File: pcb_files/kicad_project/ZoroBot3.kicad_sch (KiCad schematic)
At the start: 107 parts, among them SW1 SW_Push, SW2 SW_Push, SW3 SW_Push, SW4 SW_DIP_x02, SW5 SW_Reset, U1 TB6612FNG, U3 MP2307, Y1 Crystal

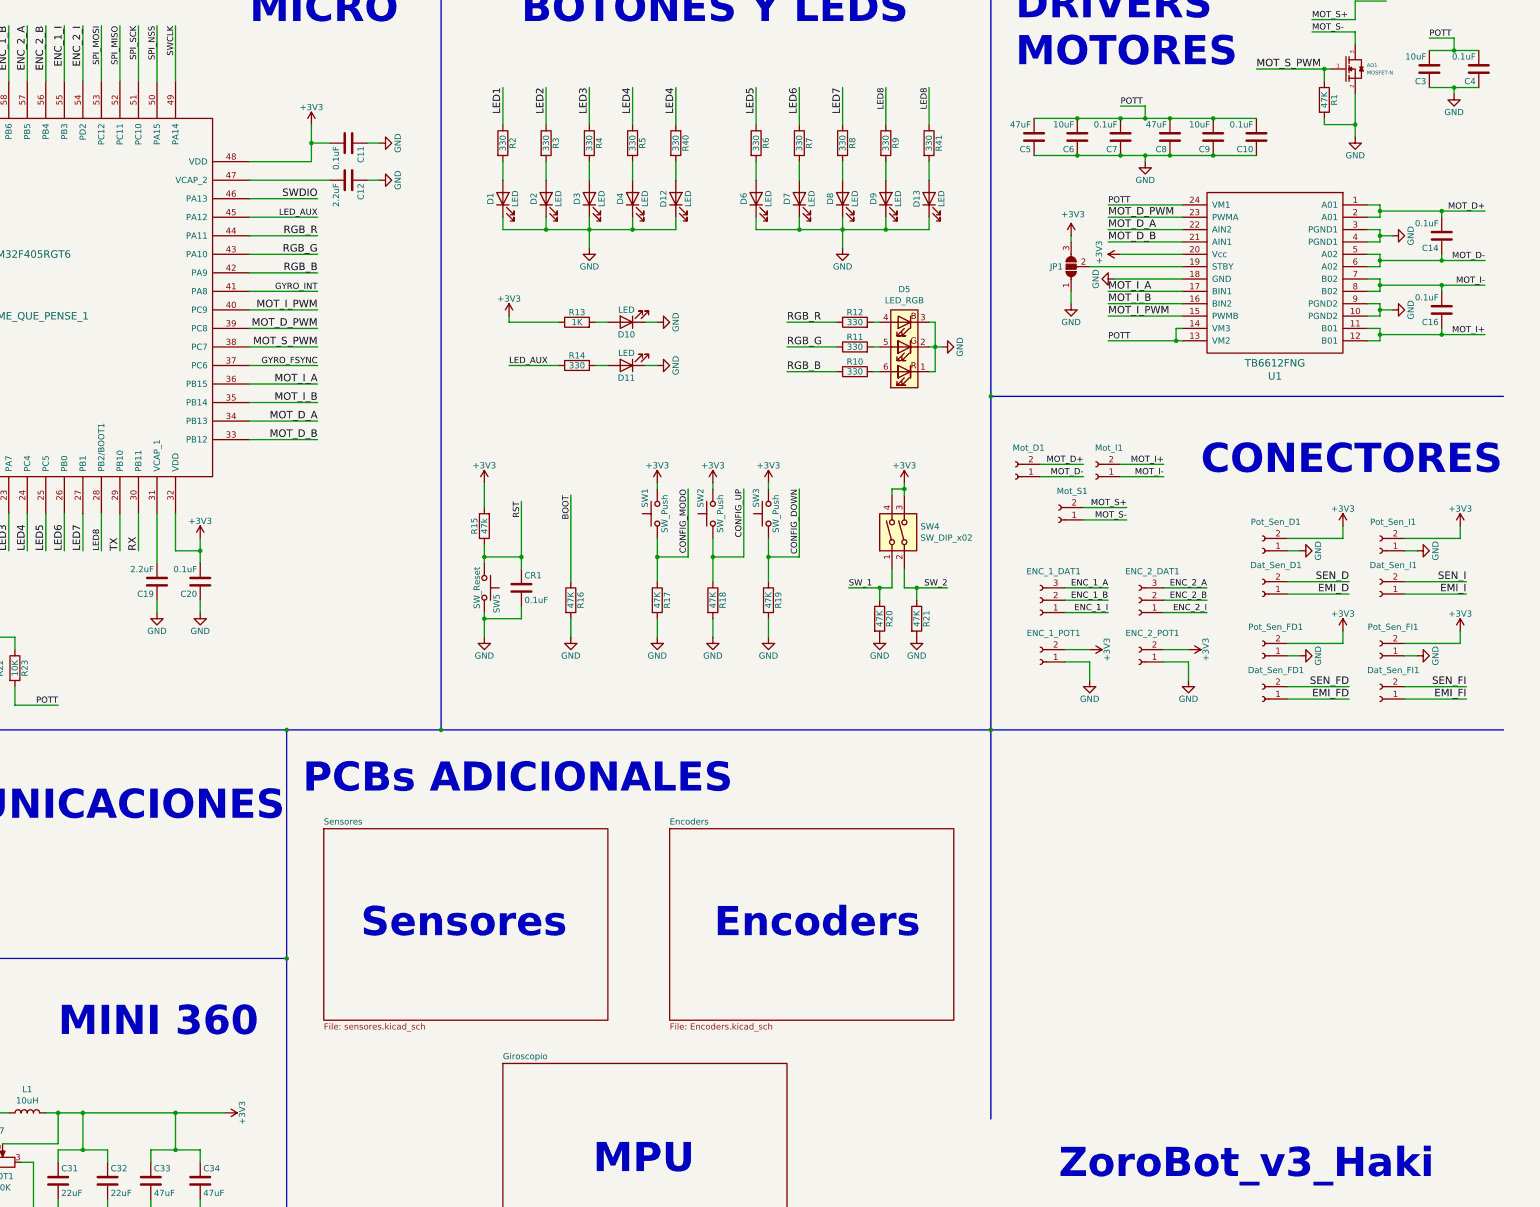
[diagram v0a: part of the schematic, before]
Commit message: Añade nuevo MPU LSM6DSR
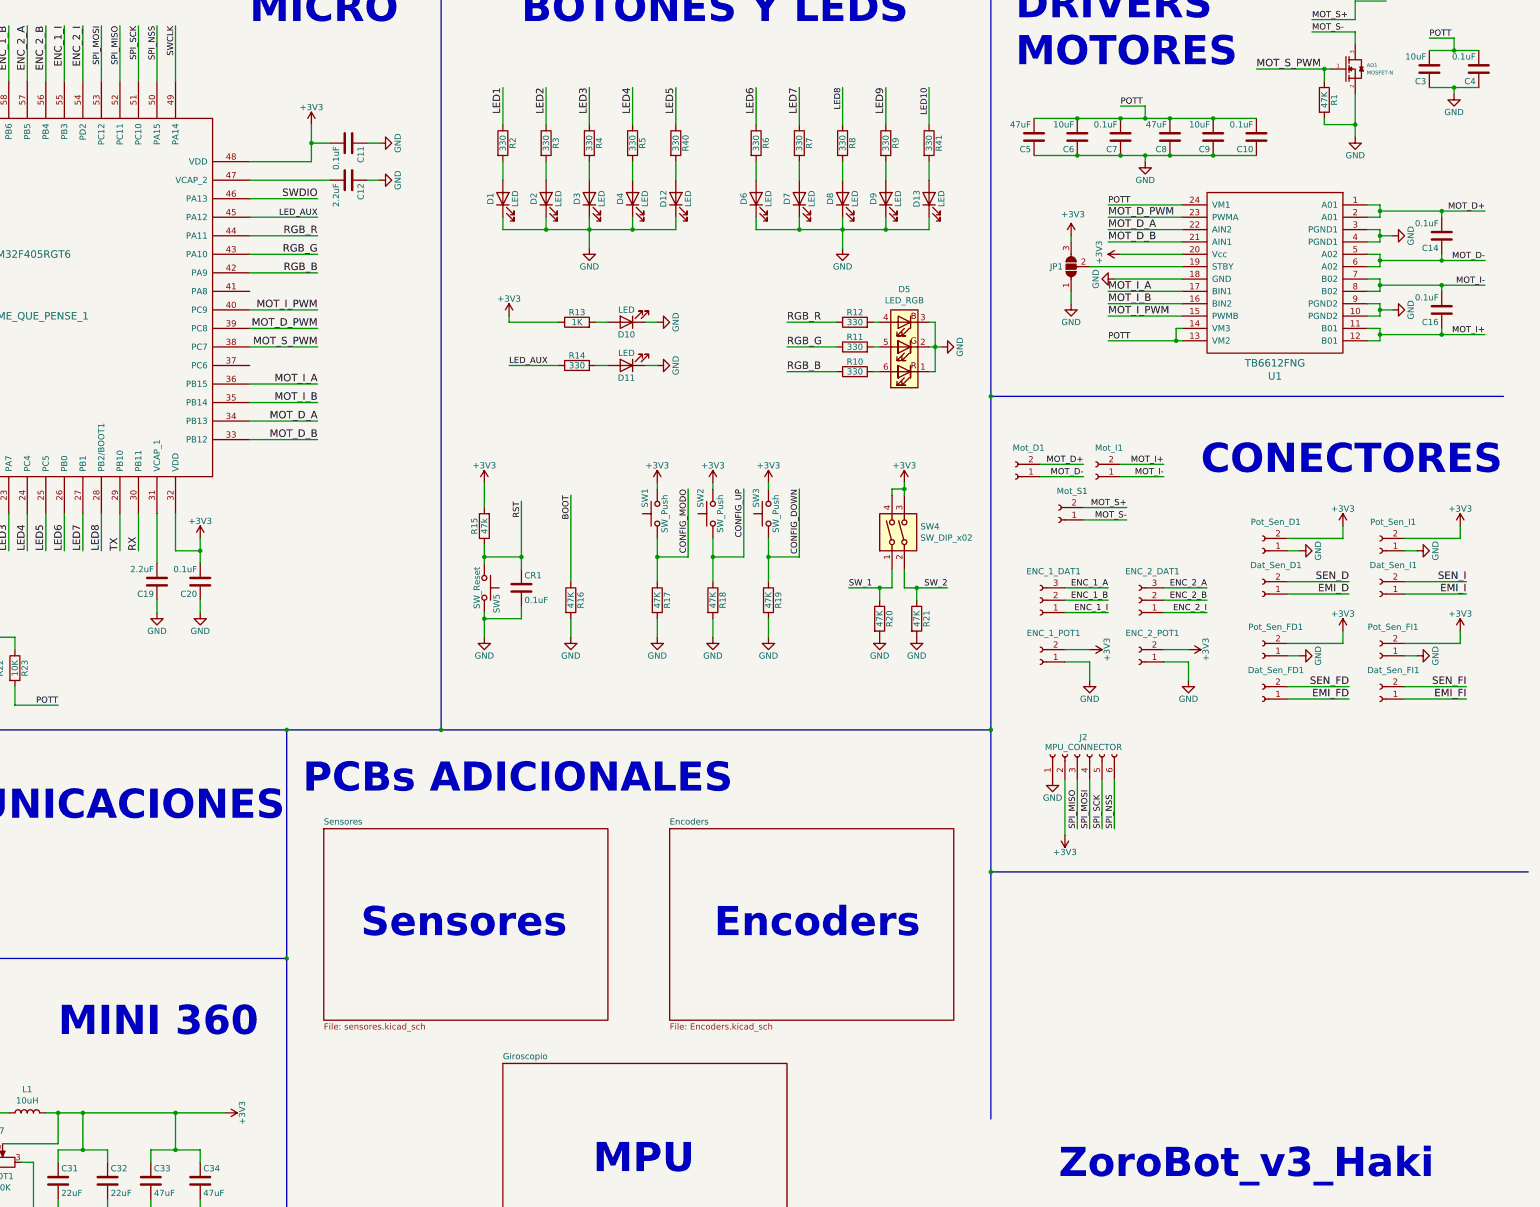
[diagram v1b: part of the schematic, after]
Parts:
- added J2: MPU_CONNECTOR, symbol Connector:Conn_01x06_Socket
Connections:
- net +3V3: now also J2.2 (Pin_2)
- net GND: now also J2.1 (Pin_1)
- net LED4: no longer R40.1
- net LED5: now also R40.1; no longer R6.1
- net LED6: now also R6.1; no longer R7.1
- net LED7: now also R7.1; no longer R8.1
- net LED8: now also R8.1; no longer R41.1, R9.1
- net SPI_MISO: now also J2.3 (Pin_3)
- net SPI_MOSI: now also J2.4 (Pin_4)
- net SPI_NSS: now also J2.6 (Pin_6)
- net SPI_SCK: now also J2.5 (Pin_5)
- net GYRO_FSYNC: no longer names the net of DEIXAME_QUE_PENSE_1.37 (PC6)
- net GYRO_INT: no longer names the net of DEIXAME_QUE_PENSE_1.41 (PA8)
- new net LED10: R41.1
- new net LED9: R9.1

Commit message: Añade receptor IR SMD TSSP77038TR
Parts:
- removed SW1, SW2, SW3: SW_Push, Button_Switch_SMD:SW_SPST_EVQPE1, symbol PCB_ZoroBot_v3-rescue:SW_Push-multiPCB-rescue-multiPCB-rescue-PCB_Fujitora-resc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
- removed SW4: SW_DIP_x02, Button_Switch_SMD:SW_DIP_SPSTx02_Slide_6.7x6.64mm_W8.61mm_P2.54mm_LowProfile, symbol Switch:SW_DIP_x02
- added AO4, AO5: MOSFET-N, Package_TO_SOT_SMD:SOT-23, symbol PCB_ZoroBot_v3-rescue:MOSFET-N-MOSFET-N
- added BATT_1: Conn_01x02_Female, custom_footprints:XT30 connector, symbol PCB_Fujitora-rescue:Conn_01x02_Female-Connector
- added BTN1, BTN2, BTN3: ~, Button_Switch_SMD:SW_Push_1P1T_NO_6x6mm_H9.5mm, symbol custom_symbols:Button
- added C49: 10uF, Capacitor_SMD:C_0805_2012Metric, symbol Device:C
- added C50, CR5, CR6: 0.1uF, Capacitor_SMD:C_0805_2012Metric, symbol Device:C
- added C51, C52, C53, CR2: 0.1uF, Capacitor_SMD:C_0805_2012Metric_Pad1.18x1.45mm_HandSolder, symbol Device:C
- added CR3, CR4: 0.1uF, Capacitor_SMD:C_0402_1005Metric_Pad0.74x0.62mm_HandSolder, symbol Device:C
- added D14: D, Diode_SMD:D_1206_3216Metric, symbol Device:D
- added DC-DC1: ~, custom_footprints:SOP8_with_gnd_pad, symbol custom_symbols:CN3903
- added IR_RECIVER1: ~, symbol custom_symbols:TSSP77038TR
- added L2: L, Inductor_SMD:L_Wuerth_HCM-7050, symbol Device:L
- added MIC5219: ~, Package_TO_SOT_SMD:SOT-23-5_HandSoldering, symbol custom_symbols:LDO_ME611C33
- added MSK12C2: SW_DPDT_x2, libs sueltas:MSK12C2, symbol Switch:SW_DPDT_x2
- added R29: 47K, Resistor_SMD:R_0805_2012Metric_Pad1.20x1.40mm_HandSolder, symbol Device:R
- added R30: 47K, Resistor_SMD:R_0805_2012Metric, symbol Device:R
- R16: value 47K -> 45K; footprint Resistor_SMD:R_0805_2012Metric -> Resistor_SMD:R_0402_1005Metric_Pad0.72x0.64mm_HandSolder
- R18: value 47K -> 100k; footprint Resistor_SMD:R_0805_2012Metric -> Resistor_SMD:R_0402_1005Metric_Pad0.72x0.64mm_HandSolder
- R19: value 47K -> 60k; footprint Resistor_SMD:R_0805_2012Metric -> Resistor_SMD:R_0402_1005Metric_Pad0.72x0.64mm_HandSolder
- R20: value 47K -> 100K; footprint Resistor_SMD:R_0805_2012Metric -> Resistor_SMD:R_0805_2012Metric_Pad1.20x1.40mm_HandSolder
- R21: footprint Resistor_SMD:R_0805_2012Metric -> Resistor_SMD:R_0805_2012Metric_Pad1.20x1.40mm_HandSolder
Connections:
- net SW_1 is gone; now on net CONFIG_MODO: R20.1
- net SW_2 is gone; now on net CONFIG_UP: R21.1
- net +3V3: now also C49.2, C50.2, IR_RECIVER1.2 (VCC)
- net BOOT: now also R17.1; no longer R16.1
- net CONFIG_DOWN: now also BTN3.1, C53.1, R29.1; no longer R19.1
- net CONFIG_MODO: now also BTN1.1, C51.1; no longer R17.1
- net CONFIG_UP: now also BTN2.1, C52.1; no longer R18.1
- net GND: now also R16.1, AO5.2, BATT_1.1 (Pin_1), C49.1, C50.1, C51.2, C52.2, C53.2, CR2.1, CR5.1, CR6.2, D14.2 (A), DC-DC1.4 (GND), DC-DC1.9 (EPAD), IR_RECIVER1.1 (GND), IR_RECIVER1.4 (GND), MIC5219.2 (VSS), R29.2, R30.2; no longer R16.2, R18.2, R19.2
- net LED10: now also DEIXAME_QUE_PENSE_1.61 (PB8)
- net LED9: now also DEIXAME_QUE_PENSE_1.62 (PB9)
- net LED_AUX: now also DEIXAME_QUE_PENSE_1.41 (PA8); no longer DEIXAME_QUE_PENSE_1.45 (PA12)
- net MOT_S-: now also AO5.3
- net MOT_S_PWM: now also AO5.1, R30.1
- net at MOSFET-P1.1, R25.2: no longer MSK12C1.3 (C)
- net AUX_PIN: now reaches DEIXAME_QUE_PENSE_1.37 (PC6)
- new net: CR4.2, DC-DC1.5 (FB), R16.2, R19.2
- new net: CR3.2, DC-DC1.1 (BST)
- new net: CR3.1, DC-DC1.3 (SW), L2.1
- new net: DC-DC1.7 (EN), R18.1
- new net +3.3V: BTN1.2, BTN2.2, BTN3.2, MIC5219.5 (VOUT)
- new net +5V: CR4.1, CR5.2, CR6.1, L2.2, MIC5219.1 (VIN), MIC5219.3 (CE), R19.1
- new net BATT: BATT_1.2 (Pin_2), CR2.2, D14.1 (K), DC-DC1.2 (VIN), R18.2
- new net IR_SENSOR: DEIXAME_QUE_PENSE_1.45 (PA12), IR_RECIVER1.3 (OUT)
- no-connect marks 2 -> 3
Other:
- note added: "regulador"
- moved on the sheet: BATT1, C26, C27, C28, C29, C30, C31, C32, C33, C34, CR1, JP2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

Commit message: Finaliza (En principio) el esquematico
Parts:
- removed AO1, AO4, AO5: MOSFET-N, Package_TO_SOT_SMD:SOT-23, symbol PCB_ZoroBot_v3-rescue:MOSFET-N-MOSFET-N
- removed BATT1: Conn_01x03_Male, Connector_JST:JST_XH_B3B-XH-A_1x03_P2.50mm_Vertical, symbol PCB_ZoroBot_v3-rescue:Conn_01x03_Male-Connector
- removed BATT_1: Conn_01x02_Female, custom_footprints:XT30 connector, symbol PCB_Fujitora-rescue:Conn_01x02_Female-Connector
- removed C31: 22uF, Capacitor_SMD:C_1206_3216Metric, symbol Device:C
- removed C34: 47uF, Capacitor_SMD:C_0805_2012Metric, symbol Device:C
- removed C51, C52, C53: 0.1uF, Capacitor_SMD:C_0805_2012Metric_Pad1.18x1.45mm_HandSolder, symbol Device:C
- removed DEIXAME_QUE_PENSE_1: STM32F405RGT6, Package_QFP:LQFP-64_10x10mm_P0.5mm, symbol PCB_ZoroBot_v3-rescue:STM32F405RGT6-stm32f405rgt6-multiPCB-rescue-PCB_Fujitora-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
- removed Dat_Sen_D1, Dat_Sen_FD1, Dat_Sen_FI1, Dat_Sen_I1, Pot_Sen_D1, Pot_Sen_FD1, Pot_Sen_FI1, Pot_Sen_I1: Conn_01x02_Female, PCB_ZoroBot_v3:Princp_Sens_Zoro, symbol PCB_ZoroBot_v3-rescue:Conn_01x02_Female-Connector
- removed ENC_1_DAT1, ENC_2_DAT1: Conn_01x03_Female, PCB_ZoroBot_v3:Princp_Dat_Encd_Zoro, symbol PCB_ZoroBot_v3-rescue:Conn_01x03_Female-Connector
- removed ENC_1_POT1, ENC_2_POT1: Conn_01x02_Female, PCB_ZoroBot_v3:Princp_Pot_Encd_Zoro, symbol PCB_ZoroBot_v3-rescue:Conn_01x02_Female-Connector
- removed JP2: SolderJumper_2_Open, Jumper:SolderJumper-2_P1.3mm_Open_RoundedPad1.0x1.5mm, symbol Jumper:SolderJumper_2_Open
- removed L1: 10uH, Inductor_SMD:L_Wuerth_HCM-7050, symbol Device:L
- removed MOSFET-P1: AO3401, Package_TO_SOT_SMD:SOT-23, symbol PCB_ZoroBot_v3-rescue:MOSFET-P-MOSFET-P
- removed MSK12C1: SW_DPDT_x2, libs sueltas:MSK12C2, symbol Switch:SW_DPDT_x2
- removed Mot_D1, Mot_I1, Mot_S1: Conn_01x02_Female, Connector_Hirose:Hirose_DF13-02P-1.25DSA_1x02_P1.25mm_Vertical, symbol PCB_ZoroBot_v3-rescue:Conn_01x02_Female-Connector
- removed POT1: 50K, Potentiometer_SMD:Potentiometer_Vishay_TS53YJ_Vertical, symbol PCB_ZoroBot_v3-rescue:R_POT-Device
- removed R25: 47K, Resistor_SMD:R_0805_2012Metric, symbol Device:R
- removed R26: 6.8K, Resistor_SMD:R_0603_1608Metric, symbol Device:R
- removed R27: 10K, Resistor_SMD:R_0603_1608Metric, symbol Device:R
- removed SW5: SW_Reset, Button_Switch_SMD:SW_SPST_EVQPE1, symbol PCB_ZoroBot_v3-rescue:SW_Push-multiPCB-rescue-multiPCB-rescue-PCB_Fujitora-resc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
- removed U1: TB6612FNG, Package_SO:SSOP-24_5.3x8.2mm_P0.65mm, symbol PCB_ZoroBot_v3-rescue:TB6612FNG-DragonBot2-cache
- removed U3: MP2307, Package_SO:SOIC-8-1EP_3.9x4.9mm_P1.27mm_EP2.41x3.3mm_ThermalVias, symbol PCB_ZoroBot_v3-rescue:MP2307-mp2307
- removed USB1: HRO-TYPE-C-31-M-12, Type-C:HRO-TYPE-C-31-M-12, symbol PCB_ZoroBot_v3-rescue:HRO-TYPE-C-31-M-12-Type-C
- added AD8418AWBZ_1, AD8418AWBZ_2: ~, symbol custom_symbols:AD8418
- added AUX_CONN, BATT1: Conn_01x03_Pin, symbol Connector:Conn_01x03_Pin
- added BTN_RST: ~, Button_Switch_SMD:SW_Push_1P1T_NO_6x6mm_H9.5mm, symbol custom_symbols:Button
- added CR7: 1uF, Capacitor_SMD:C_0805_2012Metric_Pad1.18x1.45mm_HandSolder, symbol Device:C
- added DATA_MPU, SEN_FRONT_D1, SEN_FRONT_I1, SEN_PARED_D1, SEN_PARED_I1: Conn_01x04_Socket, symbol Connector:Conn_01x04_Socket
- added DEIXAME_QUE_PENSE_1: STM32F405RGT6, Package_QFP:LQFP-64_10x10mm_P0.5mm, symbol custom_symbols:STM32F405RGT6
- added ENC_L1, ENC_R1: Conn_01x05_Socket, symbol Connector:Conn_01x05_Socket
- added JP4: SolderJumper_2_Open, Jumper:SolderJumper-2_P1.3mm_Open_RoundedPad1.0x1.5mm, symbol Jumper:SolderJumper_2_Open
- added Mot_D1, Mot_I1, Mot_S1, POWER_MPU: Conn_01x02_Socket, symbol Connector:Conn_01x02_Socket
- added PH1: ~, symbol custom_symbols:TB6612FNG
- added Q5: NMOS, symbol Simulation_SPICE:NMOS
- added Q6: AON7423, symbol Simulation_SPICE:PMOS
- added R44, R45: 0.100, symbol Device:R
- added R46: 1K, Resistor_SMD:R_0805_2012Metric, symbol Device:R
- added U1: MPU-6500, Sensor_Motion:InvenSense_QFN-24_3x3mm_P0.4mm, symbol PCB_ZoroBot_v3-rescue:MPU-6500-MPU-6500
- added USB1: ~, symbol custom_symbols:USB-C_ST-Link_USART
- C26: value 0.01uF -> 22uF; footprint Capacitor_SMD:C_0603_1608Metric -> Capacitor_SMD:C_1206_3216Metric
- C27: value 10uF -> 47uF; footprint Capacitor_SMD:C_1206_3216Metric -> Capacitor_SMD:C_0805_2012Metric
- C28: value 10uF -> 0.01uF
- C29: footprint Capacitor_SMD:C_0603_1608Metric -> Capacitor_SMD:C_0805_2012Metric
- C30: value 3.9nF -> 0.1uF; footprint Capacitor_SMD:C_0603_1608Metric -> Capacitor_SMD:C_0805_2012Metric
- R20: footprint Resistor_SMD:R_0805_2012Metric_Pad1.20x1.40mm_HandSolder -> Resistor_SMD:R_0805_2012Metric
- R21: value 47K -> 200K; footprint Resistor_SMD:R_0805_2012Metric_Pad1.20x1.40mm_HandSolder -> Resistor_SMD:R_0805_2012Metric
- R24: value 100K -> 10K; footprint Resistor_SMD:R_0603_1608Metric -> Resistor_SMD:R_0805_2012Metric
- R29: value 47K -> 47k; footprint Resistor_SMD:R_0805_2012Metric_Pad1.20x1.40mm_HandSolder -> Resistor_SMD:R_0805_2012Metric
- R30: value 47K -> 1K
- renumbered MSK12C2 to POWER_SWITCH1
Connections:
- net +3V3: now also C28.2, C30.2, MIC5219.5 (VOUT), R21.1, R29.1, AUX_CONN.2 (Pin_2), DEIXAME_QUE_PENSE_1.1 (VBAT), DEIXAME_QUE_PENSE_1.13 (VDDA), DEIXAME_QUE_PENSE_1.19 (VDD), DEIXAME_QUE_PENSE_1.32 (VDD), DEIXAME_QUE_PENSE_1.48 (VDD), DEIXAME_QUE_PENSE_1.64 (VDD), ENC_L1.2 (Pin_2), ENC_R1.2 (Pin_2), PH1.5 (A02), POWER_MPU.2 (Pin_2), R46.1, SEN_FRONT_D1.2 (Pin_2), SEN_FRONT_I1.2 (Pin_2), SEN_PARED_D1.2 (Pin_2), SEN_PARED_I1.2 (Pin_2), U1.13 (VDD), U1.8 (VDDIO), USB1.11 (VBUS), USB1.2 (VBUS)
- net +5V: now also C26.1, C27.1, AD8418AWBZ_1.6 (VDD), AD8418AWBZ_1.7 (VREF1), AD8418AWBZ_2.6 (VDD), AD8418AWBZ_2.7 (VREF1)
- net AUX_PIN: now also AUX_CONN.1 (Pin_1), DEIXAME_QUE_PENSE_1.37 (PC6)
- net BATT: now also C10.2, C3.2, C4.2, C5.2, C6.2, C7.2, C8.2, C9.2, R23.1, JP4.1 (A), Mot_S1.1 (Pin_1), PH1.1 (A01), PH1.11 (B01), PH1.12 (B01), Q6.1 (D)
- net BOOT: now also DEIXAME_QUE_PENSE_1.60 (BOOT0)
- net ENC_1_A: now also DEIXAME_QUE_PENSE_1.59 (PB7), ENC_R1.3 (Pin_3)
- net ENC_1_B: now also DEIXAME_QUE_PENSE_1.58 (PB6), ENC_R1.4 (Pin_4)
- net ENC_1_I: now also DEIXAME_QUE_PENSE_1.55 (PB3), ENC_R1.5 (Pin_5)
- net ENC_2_A: now also DEIXAME_QUE_PENSE_1.57 (PB5), ENC_L1.3 (Pin_3)
- net ENC_2_B: now also DEIXAME_QUE_PENSE_1.56 (PB4), ENC_L1.4 (Pin_4)
- net ENC_2_I: now also DEIXAME_QUE_PENSE_1.54 (PD2), ENC_L1.5 (Pin_5)
- net GND: now also C26.2, C28.1, C29.1, C30.1, POWER_SWITCH1.2 (B), R20.1, AD8418AWBZ_1.2 (GND), AD8418AWBZ_1.3 (VREF2), AD8418AWBZ_2.2 (GND), AD8418AWBZ_2.3 (VREF2), AUX_CONN.3 (Pin_3), BATT1.3 (Pin_3), BTN_RST.2, DEIXAME_QUE_PENSE_1.12 (VSSA), DEIXAME_QUE_PENSE_1.18 (VSS), DEIXAME_QUE_PENSE_1.63 (VSS), ENC_L1.1 (Pin_1), ENC_R1.1 (Pin_1), PH1.15 (PWMB), PH1.16 (BIN2), PH1.21 (AIN1), PH1.22 (AIN2), PH1.7 (B02), POWER_MPU.1 (Pin_1), Q5.3 (S), SEN_FRONT_D1.1 (Pin_1), SEN_FRONT_I1.1 (Pin_1), SEN_PARED_D1.1 (Pin_1), SEN_PARED_I1.1 (Pin_1), U1.18 (GND), U1.20 (RESV), USB1.1 (GND), USB1.12 (GND), USB1.13 (SHIELD); no longer C28.2, C29.2, R20.2, R21.2, R29.2, R30.2
- net IR_SENSOR: now also DEIXAME_QUE_PENSE_1.45 (PA12)
- net LED1: now also DEIXAME_QUE_PENSE_1.24 (PC4)
- net LED10: now also DEIXAME_QUE_PENSE_1.61 (PB8)
- net LED2: now also DEIXAME_QUE_PENSE_1.25 (PC5)
- net LED3: now also DEIXAME_QUE_PENSE_1.26 (PB0)
- net LED4: now also DEIXAME_QUE_PENSE_1.27 (PB1)
- net LED5: now also DEIXAME_QUE_PENSE_1.28 (PB2/BOOT1)
- net LED6: now also DEIXAME_QUE_PENSE_1.4 (PC15)
- net LED7: now also DEIXAME_QUE_PENSE_1.3 (PC14)
- net LED8: now also DEIXAME_QUE_PENSE_1.2 (PC13)
- net LED9: now also DEIXAME_QUE_PENSE_1.62 (PB9)
- net LED_AUX: now also DEIXAME_QUE_PENSE_1.41 (PA8)
- net MOT_D+: now also AD8418AWBZ_1.8 (+IN), Mot_D1.1 (Pin_1), R45.2; no longer C14.2
- net MOT_D-: now also Mot_D1.2 (Pin_2), PH1.19 (STBY), PH1.20 (Vcc)
- net MOT_D_A: now also DEIXAME_QUE_PENSE_1.34 (PB13), PH1.3 (PGND1)
- net MOT_D_B: now also DEIXAME_QUE_PENSE_1.33 (PB12), PH1.4 (PGND1)
- net MOT_D_PWM: now also DEIXAME_QUE_PENSE_1.39 (PC8), PH1.2 (A01)
- net MOT_I+: now also AD8418AWBZ_2.8 (+IN), Mot_I1.1 (Pin_1), R44.1; no longer C16.1
- net MOT_I-: now also Mot_I1.2 (Pin_2), PH1.17 (BIN1), PH1.18 (GND)
- net MOT_I_A: now also DEIXAME_QUE_PENSE_1.36 (PB15), PH1.8 (B02)
- net MOT_I_B: now also DEIXAME_QUE_PENSE_1.35 (PB14), PH1.9 (PGND2)
- net MOT_I_PWM: now also DEIXAME_QUE_PENSE_1.40 (PC9), PH1.10 (PGND2)
- net MOT_S-: now also Mot_S1.2 (Pin_2), Q5.1 (D)
- net MOT_S_PWM: now also DEIXAME_QUE_PENSE_1.38 (PC7), Q5.2 (G); no longer R30.1
- net RGB_B: now also DEIXAME_QUE_PENSE_1.42 (PA9)
- net RGB_G: now also DEIXAME_QUE_PENSE_1.43 (PA10)
- net RGB_R: now also DEIXAME_QUE_PENSE_1.44 (PA11)
- net RST: now also BTN_RST.1, DEIXAME_QUE_PENSE_1.7 (NRST)
- net RX: now also DEIXAME_QUE_PENSE_1.30 (PB11), USB1.6 (DP1), USB1.8 (DP2)
- net SPI_MISO: now also DATA_MPU.1 (Pin_1), DEIXAME_QUE_PENSE_1.52 (PC11), U1.9 (AD0/SDO)
- net SPI_MOSI: now also DATA_MPU.2 (Pin_2), DEIXAME_QUE_PENSE_1.53 (PC12), U1.24 (SDA/SDI)
- net SPI_NSS: now also DATA_MPU.4 (Pin_4), DEIXAME_QUE_PENSE_1.50 (PA15), U1.22 (nCS)
- net SPI_SCK: now also DATA_MPU.3 (Pin_3), DEIXAME_QUE_PENSE_1.51 (PC10), U1.23 (SCL/SCLK)
- net SWCLK: now also DEIXAME_QUE_PENSE_1.49 (PA14), USB1.10 (CC2), USB1.4 (CC1)
- net SWDIO: now also DEIXAME_QUE_PENSE_1.46 (PA13), USB1.3 (SBU2), USB1.9 (SBU1)
- net TX: now also DEIXAME_QUE_PENSE_1.29 (PB10), USB1.5 (DN2), USB1.7 (DN1)
- net at C15.2, Y1.1: now also DEIXAME_QUE_PENSE_1.6 (PH1/OSC_OUT)
- net at C13.2, Y1.2: now also DEIXAME_QUE_PENSE_1.5 (PH0/OSC_IN)
- net at C19.2: now also DEIXAME_QUE_PENSE_1.31 (VCAP_1)
- net at C12.2: now also DEIXAME_QUE_PENSE_1.47 (VCAP_2)
- net BATT_VOLTAGE: now reaches R22.1
- net BATT_VOLTAGE: now also R23.2, DEIXAME_QUE_PENSE_1.20 (PA4); no longer R23.1
- net at JP1.2 (C): now also PH1.6 (A02)
- net LIPO+: now reaches R24.2
- net LIPO+: now also BATT1.1 (Pin_1), CR7.1, JP4.2 (B), Q6.3 (S)
- net at POWER_SWITCH1.3 (C): now also R24.1, R30.1
- net +3.3V renamed MENU_ANALOG
- net MENU_ANALOG: now also R20.2, DEIXAME_QUE_PENSE_1.23 (PA7); no longer MIC5219.5 (VOUT)
- net CONFIG_DOWN: no longer names the net of BTN3.1
- net CONFIG_DOWN: now also R46.2; no longer R29.1
- net CONFIG_MODO: no longer names the net of BTN1.1
- net CONFIG_MODO: now also R21.2; no longer R20.1
- net CONFIG_UP: no longer names the net of BTN2.1
- net CONFIG_UP: now also R29.2; no longer R21.1
- removed net MOT_S+: C10.2, C27.1, C28.1, C3.2, C4.2, C5.2, C6.2, C7.2, C8.2, C9.2, R23.2, R24.1
- new net: CR7.2, Q6.2 (G), R30.2
- new net: C29.2, U1.10 (REGOUT)
- new net CURR_SEN_MD: AD8418AWBZ_1.5 (OUT), DEIXAME_QUE_PENSE_1.21 (PA5)
- new net CURR_SEN_MI: AD8418AWBZ_2.5 (OUT), DEIXAME_QUE_PENSE_1.22 (PA6)
- new net EMI_FRONT_D: DEIXAME_QUE_PENSE_1.17 (PA3), SEN_FRONT_D1.4 (Pin_4)
- new net EMI_FRONT_I: DEIXAME_QUE_PENSE_1.14 (PA0), SEN_FRONT_I1.4 (Pin_4)
- new net EMI_PA_D: DEIXAME_QUE_PENSE_1.15 (PA1), SEN_PARED_D1.4 (Pin_4)
- new net EMI_PA_I: DEIXAME_QUE_PENSE_1.16 (PA2), SEN_PARED_I1.4 (Pin_4)
- new net SEN_FRONT_D: DEIXAME_QUE_PENSE_1.11 (PC3), SEN_FRONT_D1.3 (Pin_3)
- new net SEN_FRONT_I: DEIXAME_QUE_PENSE_1.8 (PC0), SEN_FRONT_I1.3 (Pin_3)
- new net SEN_PA_D: DEIXAME_QUE_PENSE_1.9 (PC1), SEN_PARED_D1.3 (Pin_3)
- new net SEN_PA_I: DEIXAME_QUE_PENSE_1.10 (PC2), SEN_PARED_I1.3 (Pin_3)
- new net SHUNT_MD: AD8418AWBZ_1.1 (-IN), C14.2, PH1.23 (PWMA), PH1.24 (VM1), R45.1
- new net SHUNT_MI: AD8418AWBZ_2.1 (-IN), C16.1, PH1.13 (VM2), PH1.14 (VM3), R44.2
- no-connect marks 3 -> 7
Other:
- note added: "ALIMENTACIÓN"
- note added: "LEDS Y BOTONES"
- note added: "MICROCONTROLADOR"
- note added: "MPU-6500"
- note added: "MPUs"
- note removed: "BOTONES Y LEDS"
- note removed: "MICRO"
- note removed: "MINI 360"
- note removed: "MPU"
- moved on the sheet: C1, C10, C13, C14, C15, C16, C2, C32, C33, C49, C5, C50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
